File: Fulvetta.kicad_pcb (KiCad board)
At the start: 2 copper layers, 75 x 82 mm, 41 parts, among them J1 Conn_02x05_Odd_Even, J10 Conn_02x05_Odd_Even, J2 Conn_02x05_Odd_Even, J3 Conn_02x05_Odd_Even, J4 Conn_02x05_Odd_Even, J5 Conn_02x05_Odd_Even, J6 Conn_02x05_Odd_Even, J7 Conn_02x05_Odd_Even, J8 Conn_02x05_Odd_Even, J9 Conn_02x05_Odd_Even, U1 MAX4617EUE+, U10 MAX4617EUE+, U11 Digilent-CoraZ7_units, U2 MAX4617EUE+, U3 MAX4617EUE+, U4 MAX4617EUE+, U5 MAX4617EUE+, U6 MAX4617EUE+, U7 MAX4617EUE+, U8 MAX4617EUE+, U9 MAX4617EUE+

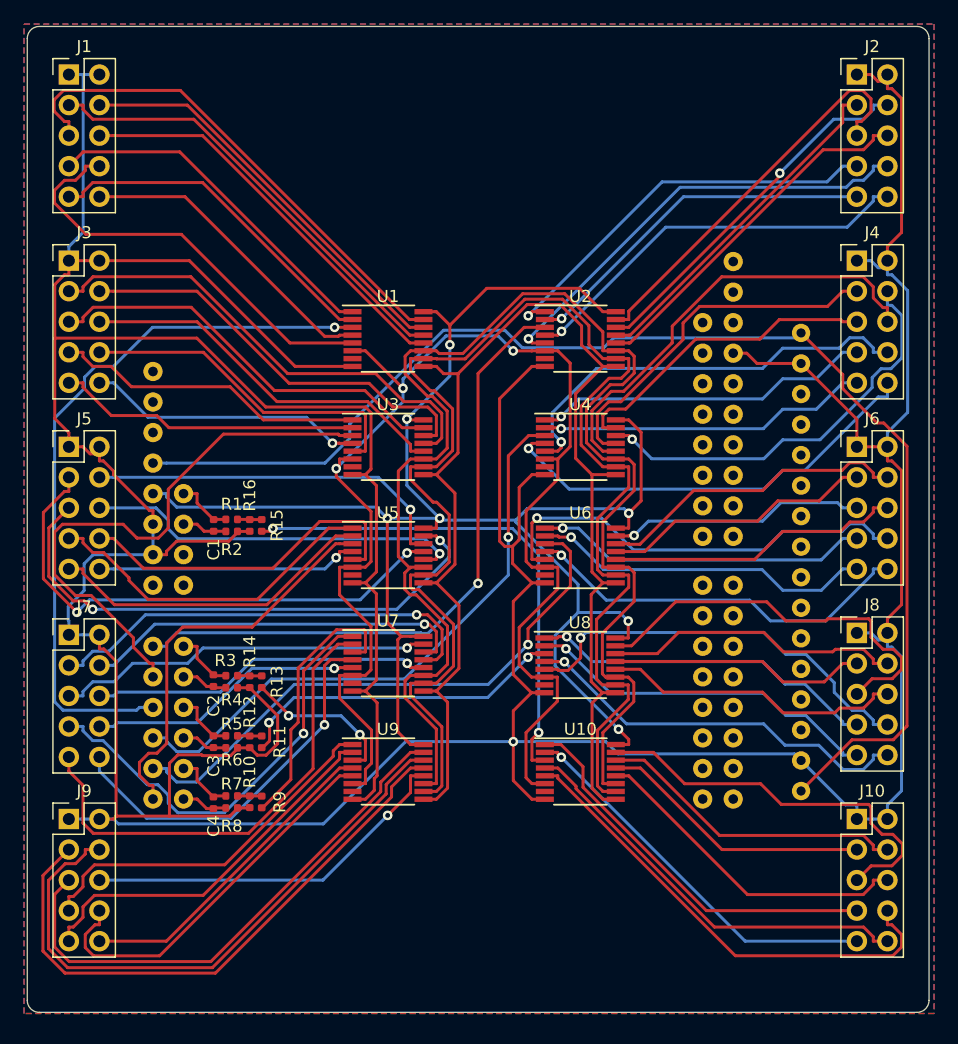
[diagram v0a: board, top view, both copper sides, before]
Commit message: reduced board size from top and bottom
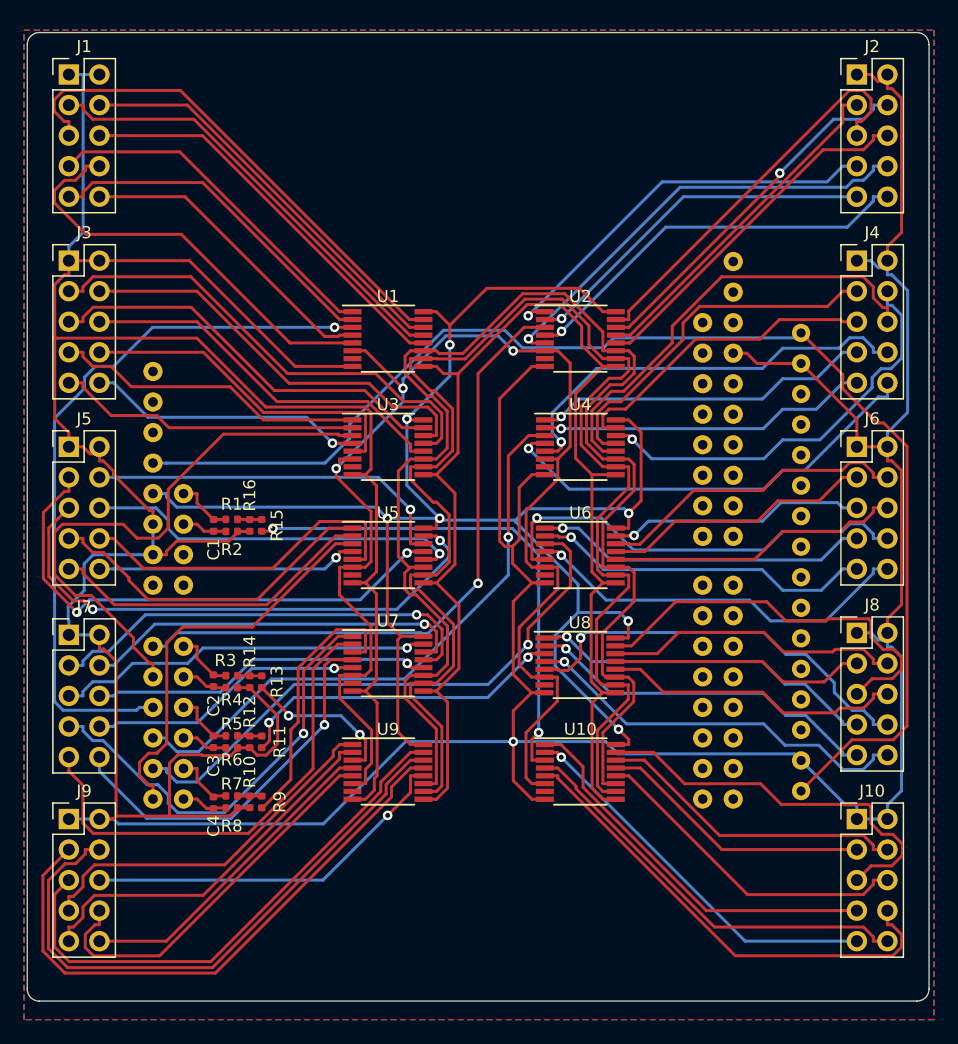
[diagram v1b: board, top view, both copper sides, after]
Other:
- board size 75 x 82 mm -> 75 x 80.6 mm
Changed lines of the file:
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@@
     (32 B.Adhes user)
     (33 F.Adhes user)
-    (34 B.Paste user)
+    (34 B.Paste user hide)
     (35 F.Paste user)
     (36 B.SilkS user)
@@
     (38 B.Mask user)
     (39 F.Mask user)
-    (40 Dwgs.User user)
+    (40 Dwgs.User user hide)
     (41 Cmts.User user)
     (42 Eco1.User user)
@@
     )
   )
-  (gr_arc (start 143 132) (end 142 132) (angle -90) (layer Edge.Cuts) (width 0.05))
-  (gr_arc (start 216 132) (end 216 133) (angle -90) (layer Edge.Cuts) (width 0.05))
-  (gr_arc (start 216 52) (end 217 52) (angle -90) (layer Edge.Cuts) (width 0.05))
-  (gr_arc (start 143 52) (end 143 51) (angle -90) (layer Edge.Cuts) (width 0.05))
-  (gr_line (start 142 132) (end 142 52) (layer Edge.Cuts) (width 0.05))
-  (gr_line (start 216 133) (end 143 133) (layer Edge.Cuts) (width 0.05))
-  (gr_line (start 217 52) (end 217 132) (layer Edge.Cuts) (width 0.05))
-  (gr_line (start 143 51) (end 216 51) (layer Edge.Cuts) (width 0.05))
+  (gr_line (start 143 132.064) (end 216 132.064) (layer Edge.Cuts) (width 0.05))
+  (gr_arc (start 143 131.064) (end 142 131.064) (angle -90) (layer Edge.Cuts) (width 0.05))
+  (gr_arc (start 216 131.064) (end 216 132.064) (angle -90) (layer Edge.Cuts) (width 0.05))
+  (gr_arc (start 216 52.508) (end 217 52.508) (angle -90) (layer Edge.Cuts) (width 0.05))
+  (gr_arc (start 143 52.508) (end 143 51.508) (angle -90) (layer Edge.Cuts) (width 0.05))
+  (gr_line (start 142 131.064) (end 142 52.508) (layer Edge.Cuts) (width 0.05))
+  (gr_line (start 217 52.508) (end 217 131.064) (layer Edge.Cuts) (width 0.05))
+  (gr_line (start 143 51.508) (end 216 51.508) (layer Edge.Cuts) (width 0.05))
   (segment (start 186.4377 76.3626) (end 195.105 67.6953) (width 0.25) (layer B.Cu) (net 25))
   (segment (start 195.105 67.6953) (end 210.1968 67.6953) (width 0.25) (layer B.Cu) (net 25))
@@
     (polygon
       (pts
-        (xy 217.424 133.096) (xy 141.732 133.096) (xy 141.732 50.8) (xy 217.424 50.8)
+        (xy 217.424 133.604) (xy 141.732 133.604) (xy 141.732 51.308) (xy 217.424 51.308)
       )
     )
@@
     (polygon
       (pts
-        (xy 217.424 133.096) (xy 141.732 133.096) (xy 141.732 50.8) (xy 217.424 50.8)
+        (xy 217.424 133.604) (xy 141.732 133.604) (xy 141.732 51.308) (xy 217.424 51.308)
       )
     )

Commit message: update copper pour
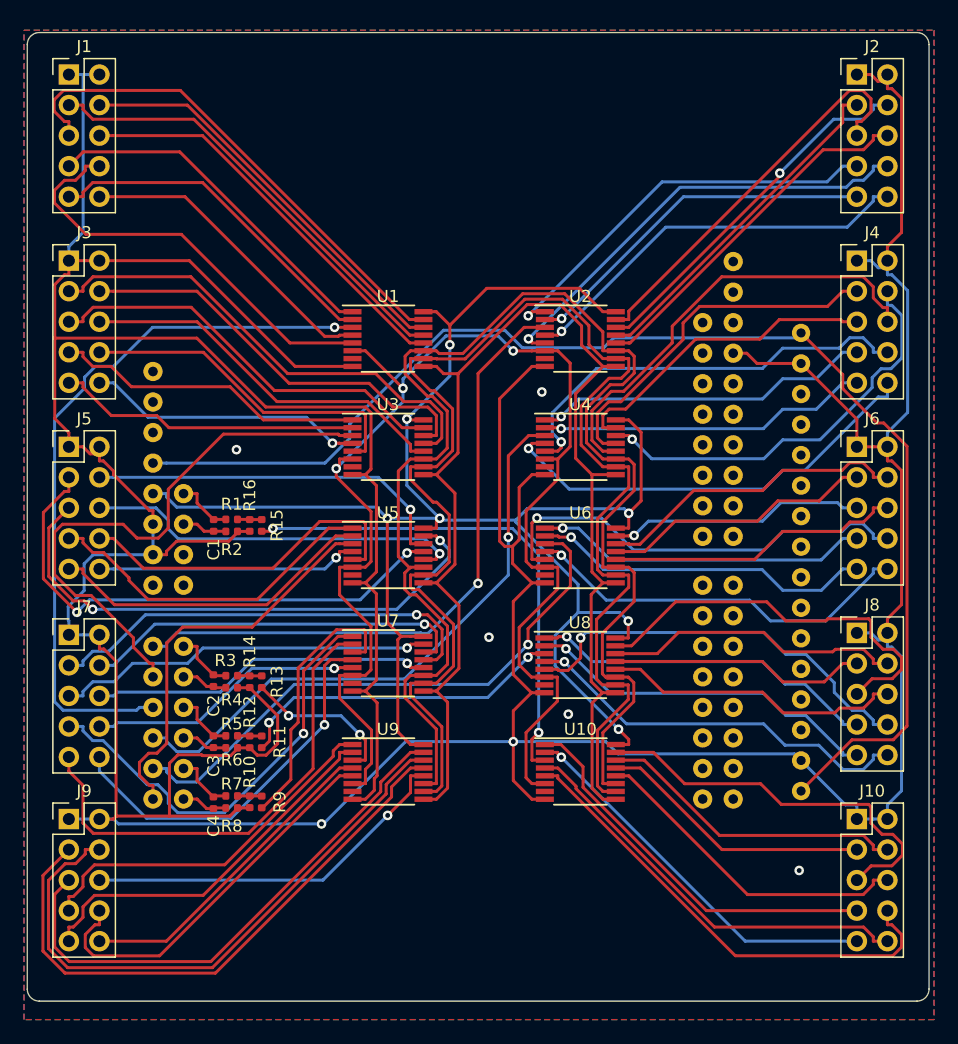
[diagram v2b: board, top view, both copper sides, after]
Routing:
- net GND: vias 1 -> 7
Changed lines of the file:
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@@
     (thickness 1.6)
     (drawings 8)
-    (tracks 1388)
+    (tracks 1395)
     (zones 0)
     (modules 41)
@@
     (38 B.Mask user)
     (39 F.Mask user)
-    (40 Dwgs.User user hide)
+    (40 Dwgs.User user)
     (41 Cmts.User user)
     (42 Eco1.User user)
@@
       (outputformat 1)
       (mirror false)
-      (drillshape 1)
+      (drillshape 0)
       (scaleselection 1)
-      (outputdirectory ""))
+      (outputdirectory "Gerber/"))
   )
   (net 0 "")
@@
   (segment (start 213.54 116.92) (end 212.3647 116.92) (width 0.25) (layer B.Cu) (net 33))
   (segment (start 149.1753 116.92) (end 149.5831 117.3278) (width 0.25) (layer B.Cu) (net 33))
-  (segment (start 149.5831 117.3278) (end 166.6208 117.3278) (width 0.25) (layer B.Cu) (net 33))
+  (segment (start 149.5831 117.3278) (end 166.4722 117.3278) (width 0.25) (layer B.Cu) (net 33))
   (segment (start 166.6208 117.3278) (end 173.4673 110.4813) (width 0.25) (layer B.Cu) (net 33))
   (segment (start 173.4673 110.4813) (end 182.4241 110.4813) (width 0.25) (layer B.Cu) (net 33))
@@
   (segment (start 214.7153 68.1294) (end 213.54 69.3047) (width 0.25) (layer F.Cu) (net 33))
   (via (at 182.4241 110.4813) (size 0.8) (layers F.Cu B.Cu) (net 33))
+  (via (at 184.8 81.4) (size 0.8) (drill 0.4) (layers F.Cu B.Cu) (net 33))
+  (via (at 159.4 86.2) (size 0.8) (drill 0.4) (layers F.Cu B.Cu) (net 33))
+  (segment (start 166.4722 117.3278) (end 166.6208 117.3278) (width 0.25) (layer B.Cu) (net 33))
+  (via (at 166.4722 117.3278) (size 0.8) (drill 0.4) (layers F.Cu B.Cu) (net 33))
+  (via (at 206.2 121.2) (size 0.8) (drill 0.4) (layers F.Cu B.Cu) (net 33))
+  (via (at 187 108.2) (size 0.8) (drill 0.4) (layers F.Cu B.Cu) (net 33))
+  (via (at 180.4 101.8) (size 0.8) (drill 0.4) (layers F.Cu B.Cu) (net 33))
   (segment (start 176.0253 104.975) (end 176.9513 104.049) (width 0.25) (layer F.Cu) (net 34))
   (segment (start 176.9513 104.049) (end 176.9513 100.877) (width 0.25) (layer F.Cu) (net 34))

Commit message: added logo
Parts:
- added G***: LOGO, footprint:HPPSI_02_logo, F.Cu at (167.6, 56.3)
- added G***: LOGO, footprint:UiO_DoM, F.Cu at (178.4, 66.0)
